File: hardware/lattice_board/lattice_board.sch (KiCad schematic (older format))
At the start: 1 part

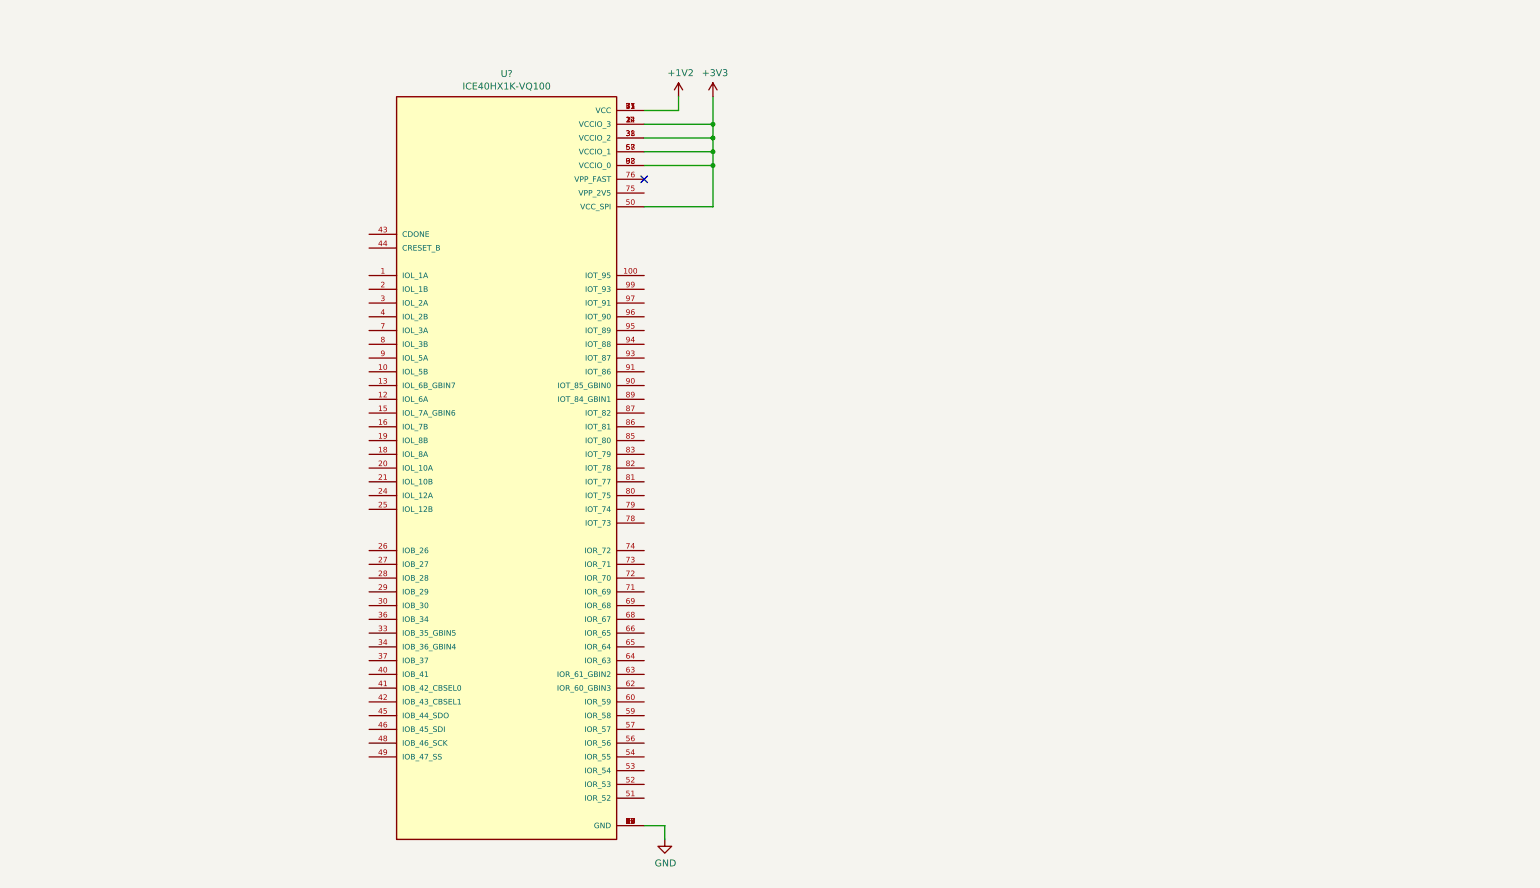
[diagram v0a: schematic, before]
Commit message: Remove .lib files from gitignore; they're important and used by KiCad
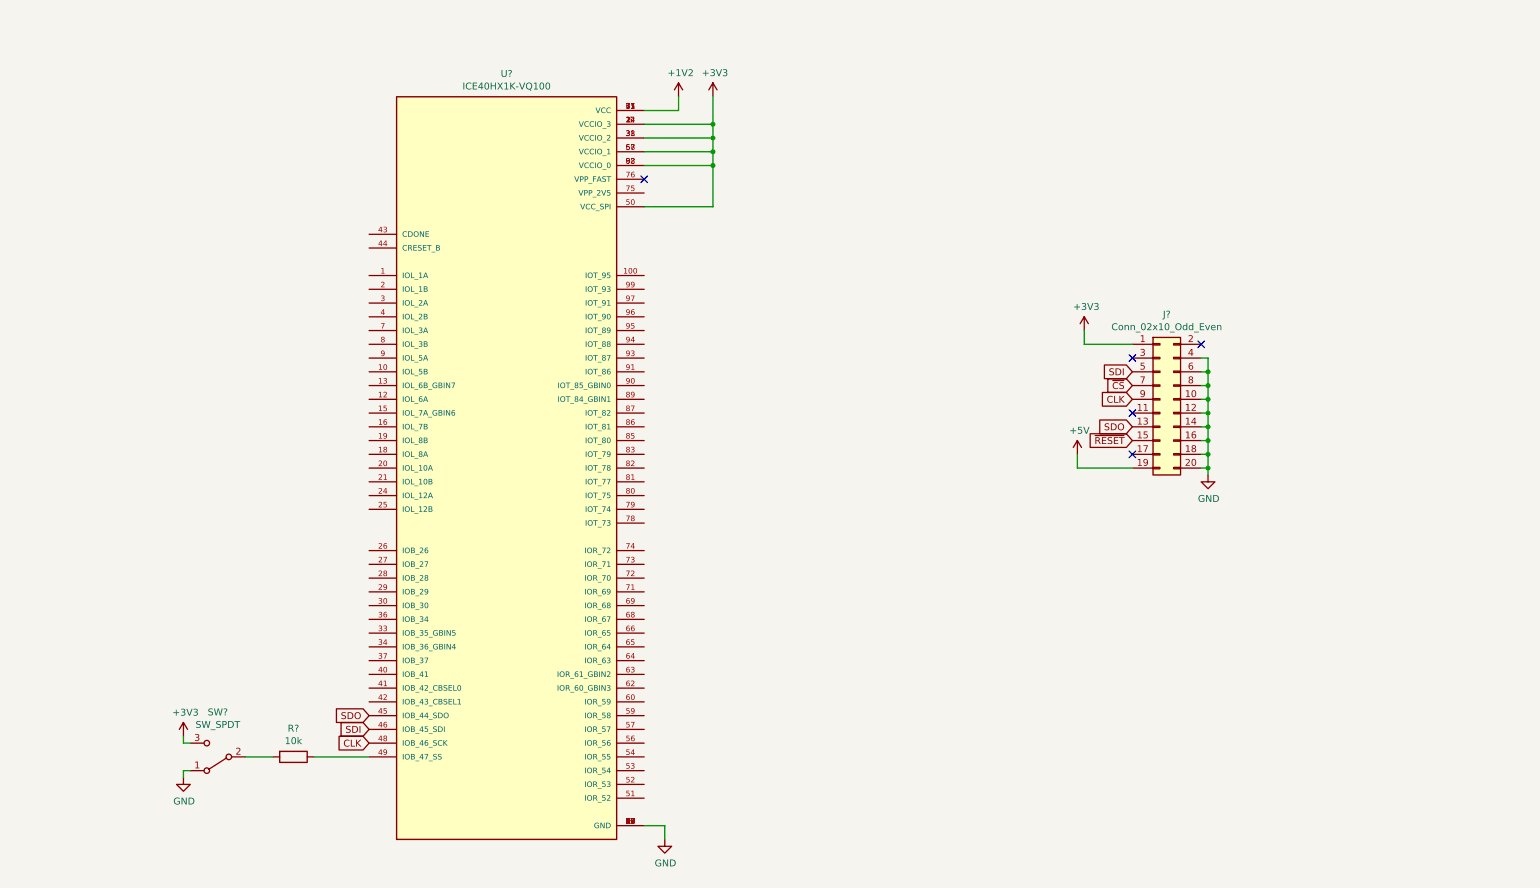
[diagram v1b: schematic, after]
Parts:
- added J?: Conn_02x10_Odd_Even, symbol Connector_Generic:Conn_02x10_Odd_Even
- added R?: 10k, symbol Device:R
- added SW?: SW_SPDT, symbol Switch:SW_SPDT
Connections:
- net +3V3: now also J?.1 (Pin_1), SW?.3 (C)
- net GND: now also J?.10 (Pin_10), J?.12 (Pin_12), J?.14 (Pin_14), J?.16 (Pin_16), J?.18 (Pin_18), J?.20 (Pin_20), J?.4 (Pin_4), J?.6 (Pin_6), J?.8 (Pin_8), SW?.1 (A)
- net SDO: now reaches U?.45 (IOB_44_SDO)
- net SDO: now also J?.13 (Pin_13)
- net SDI: now reaches U?.46 (IOB_45_SDI)
- net SDI: now also J?.5 (Pin_5)
- net CLK: now reaches U?.48 (IOB_46_SCK)
- net CLK: now also J?.9 (Pin_9)
- net at U?.49 (IOB_47_SS): now also R?.1
- new net: R?.2, SW?.2 (B)
- new net +5V: J?.19 (Pin_19)
- new net ~CS: J?.7 (Pin_7)
- new net ~RESET: J?.15 (Pin_15)
- no-connect marks 1 -> 5
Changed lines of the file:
@@
 Connection ~ 5550 1700
 NoConn ~ 5050 1800
+NoConn ~ 8600 3100
+NoConn ~ 9100 3000
+NoConn ~ 8600 3800
+$Comp
+L power:GND #PWR?
+U 1 1 60DF5C29
+P 9150 3950
+F 0 "#PWR?" H 9150 3700 50  0001 C CNN
+F 1 "GND" H 9155 3777 50  0000 C CNN
+F 2 "" H 9150 3950 50  0001 C CNN
+F 3 "" H 9150 3950 50  0001 C CNN
+	1    9150 3950
+	1    0    0    -1
+$EndComp
+Wire Wire Line
+	9150 3950 9150 3900
+Wire Wire Line
+	9150 3900 9100 3900
+Wire Wire Line
+	9100 3800 9150 3800
+Wire Wire Line
+	9150 3800 9150 3900
+Connection ~ 9150 3900
+Wire Wire Line
+	9100 3700 9150 3700
+Wire Wire Line
+	9150 3700 9150 3800
+Connection ~ 9150 3800
+Wire Wire Line
+	9100 3600 9150 3600
+Wire Wire Line
+	9150 3600 9150 3700
+Connection ~ 9150 3700
+Wire Wire Line
+	9100 3500 9150 3500
+Wire Wire Line
+	9150 3500 9150 3600
+Connection ~ 9150 3600
+Wire Wire Line
+	9100 3400 9150 3400
+Wire Wire Line
+	9150 3400 9150 3500
+Connection ~ 9150 3500
+Wire Wire Line
+	9100 3300 9150 3300
+Wire Wire Line
+	9150 3300 9150 3400
+Connection ~ 9150 3400
+Wire Wire Line
+	9100 3200 9150 3200
+Wire Wire Line
+	9150 3200 9150 3300
+Connection ~ 9150 3300
+Wire Wire Line
+	9100 3100 9150 3100
+Wire Wire Line
+	9150 3100 9150 3200
+Connection ~ 9150 3200
+$Comp
+L power:+3V3 #PWR?
+U 1 1 60DF96CA
+P 8250 2900
+F 0 "#PWR?" H 8250 2750 50  0001 C CNN
+F 1 "+3V3" H 8265 3073 50  0000 C CNN
+F 2 "" H 8250 2900 50  0001 C CNN
+F 3 "" H 8250 2900 50  0001 C CNN
+	1    8250 2900
+	1    0    0    -1
+$EndComp
+Wire Wire Line
+	8250 2900 8250 3000
+Wire Wire Line
+	8250 3000 8600 3000
+Text GLabel 8600 3200 0    50   Input ~ 0
+SDI
+Text GLabel 8600 3300 0    50   Input ~ 0
+~CS
+Text GLabel 8600 3400 0    50   Input ~ 0
+CLK
+$Comp
+L Connector_Generic:Conn_02x10_Odd_Even J?
+U 1 1 60DFD5AD
+P 8800 3400
+F 0 "J?" H 8850 4017 50  0000 C CNN
+F 1 "Conn_02x10_Odd_Even" H 8850 3926 50  0000 C CNN
+F 2 "" H 8800 3400 50  0001 C CNN
+F 3 "~" H 8800 3400 50  0001 C CNN
+	1    8800 3400
+	1    0    0    -1
+$EndComp
+NoConn ~ 8600 3500
+Text GLabel 8600 3600 0    50   Input ~ 0
+SDO
+Text GLabel 8600 3700 0    50   Input ~ 0
+~RESET
+$Comp
+L power:+5V #PWR?
+U 1 1 60DFF9BF
+P 8200 3800
+F 0 "#PWR?" H 8200 3650 50  0001 C CNN
+F 1 "+5V" H 8215 3973 50  0000 C CNN
+F 2 "" H 8200 3800 50  0001 C CNN
+F 3 "" H 8200 3800 50  0001 C CNN
+	1    8200 3800
+	1    0    0    -1
+$EndComp
+Wire Wire Line
+	8200 3800 8200 3900
+Wire Wire Line
+	8200 3900 8600 3900
+Text GLabel 3050 5800 0    50   Input ~ 0
+SDI
+Text GLabel 3050 5900 0    50   Input ~ 0
+CLK
+Text GLabel 3050 5700 0    50   Input ~ 0
+SDO
+$Comp
+L Switch:SW_SPDT SW?
+U 1 1 60E198BD
+P 1950 6000
+F 0 "SW?" H 1950 5675 50  0000 C CNN
+F 1 "SW_SPDT" H 1950 5766 50  0000 C CNN
+F 2 "" H 1950 6000 50  0001 C CNN
+F 3 "~" H 1950 6000 50  0001 C CNN
+	1    1950 6000
+	-1   0    0    1
+$EndComp
+Wire Wire Line
+	2650 6000 3050 6000
+$Comp
+L power:GND #PWR?
+U 1 1 60E1ADAD
+P 1700 6150
+F 0 "#PWR?" H 1700 5900 50  0001 C CNN
+F 1 "GND" H 1705 5977 50  0000 C CNN
+F 2 "" H 1700 6150 50  0001 C CNN
+F 3 "" H 1700 6150 50  0001 C CNN
+	1    1700 6150
+	1    0    0    -1
+$EndComp
+$Comp
+L power:+3V3 #PWR?
+U 1 1 60E1B359
+P 1700 5850
+F 0 "#PWR?" H 1700 5700 50  0001 C CNN
+F 1 "+3V3" H 1715 6023 50  0000 C CNN
+F 2 "" H 1700 5850 50  0001 C CNN
+F 3 "" H 1700 5850 50  0001 C CNN
+	1    1700 5850
+	1    0    0    -1
+$EndComp
+Wire Wire Line
+	1700 5850 1700 5900
+Wire Wire Line
+	1700 5900 1750 5900
+Wire Wire Line
+	1750 6100 1700 6100
+Wire Wire Line
+	1700 6100 1700 6150
+$Comp
+L Device:R R?
+U 1 1 60E2544C
+P 2500 6000
+F 0 "R?" V 2293 6000 50  0000 C CNN
+F 1 "10k" V 2384 6000 50  0000 C CNN
+F 2 "" V 2430 6000 50  0001 C CNN
+F 3 "~" H 2500 6000 50  0001 C CNN
+	1    2500 6000
+	0    1    1    0
+$EndComp
+Wire Wire Line
+	2350 6000 2150 6000
 $EndSCHEMATC

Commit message: Work on lattice board
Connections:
- net +2V5: now reaches U?.75 (VPP_2V5)
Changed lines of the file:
@@
 Wire Wire Line
 	2350 6000 2150 6000
+$Comp
+L power:+2V5 #PWR?
+U 1 1 60DFCED5
+P 5650 1800
+F 0 "#PWR?" H 5650 1650 50  0001 C CNN
+F 1 "+2V5" H 5665 1973 50  0000 C CNN
+F 2 "" H 5650 1800 50  0001 C CNN
+F 3 "" H 5650 1800 50  0001 C CNN
+	1    5650 1800
+	1    0    0    -1
+$EndComp
+Wire Wire Line
+	5650 1800 5650 1900
+Wire Wire Line
+	5650 1900 5050 1900
 $EndSCHEMATC

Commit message: Work on lattice board; add TODO list to lattice board
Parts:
- added D?: LS R976-NR-1 (RED), symbol Device:LED
- added Q?: ZXMN3A01F, Package_TO_SOT_SMD:SOT-23, symbol Transistor_FET:ZXMN3A01F
- added R? (x4): 10k, symbol Device:R
- added R?: 220, symbol Device:R
- added SW?: SW_Push, symbol Switch:SW_Push
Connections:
- net +3V3: now also R?.1, R?.1, R?.1, R?.1, R?.1
- net GND: now also Q?.2 (S), SW?.1
- net SDI: now also R?.2
- net SDO: now also R?.2
- net ~RESET: now also U?.44 (CRESET_B), R?.2, SW?.2
- net CDONE: now reaches U?.43 (CDONE)
- net CDONE: now also Q?.1 (G), R?.2
- net SS: now reaches R?.1, U?.49 (IOB_47_SS)
- new net: D?.1 (K), Q?.3 (D)
- new net: D?.2 (A), R?.2
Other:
- note added: "TODO:\n1.2V Core PSU\n3.3V I/O + SPI PSU\n2.5V NVP PSU\nSTEMMA/Qwiic Header\nExpansion Headers(Hirose DF9-41S/P-1V-32)\nExpansion Boards(GPIO, PMOD, VGA, button, LED)\nDRAM (IS42S16100H-7TLI)\nDVI/HDMI\nButtons\nLEDs\n7-seg\nEthernet\nUSB Host"
- moved on the sheet: R?, SW?, U?
